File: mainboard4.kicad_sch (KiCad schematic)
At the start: 14 parts, among them J13 USB_C_Receptacle_USB2.0_16P, J8 Barrel_Jack

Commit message: change cad data
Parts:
- removed C103, C104: 0.1uF, Capacitor_SMD:C_0402_1005Metric_Pad0.74x0.62mm_HandSolder, symbol Device:C
- renumbered C80 to C107, C81 to C108, C82 to C109, C83 to C110, C101 to C125, C102 to C126, C42 to C64, C43 to C65, C44 to C66, C45 to C67
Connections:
- net USB HUB/SS_RX_N is gone; now on net USB HUB/SS_TX_N: C126.1
- net USB HUB/SS_RX_P is gone; now on net USB HUB/SS_TX_P: C125.1
- net Ethernet PHY/RXN: now also C66.2; no longer C64.2
- net Ethernet PHY/RXP: now also C67.2; no longer C65.2
- net Ethernet PHY/TXN: now also C64.2; no longer C66.2
- net Ethernet PHY/TXP: now also C65.2; no longer C67.2
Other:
- added sheet IMU (imu.kicad_sch)
- sheet MCU ports: added CS, INT, MISO, MOSI, RST, SCLK, USB_DN, USB_DP; removed none
- sheet USB2Ethernet ports: added USB2DM, USB2DP; removed none
- moved on the sheet: C107, C109, C110, C125, C126, C64, C65, C66, C67, J13, J8

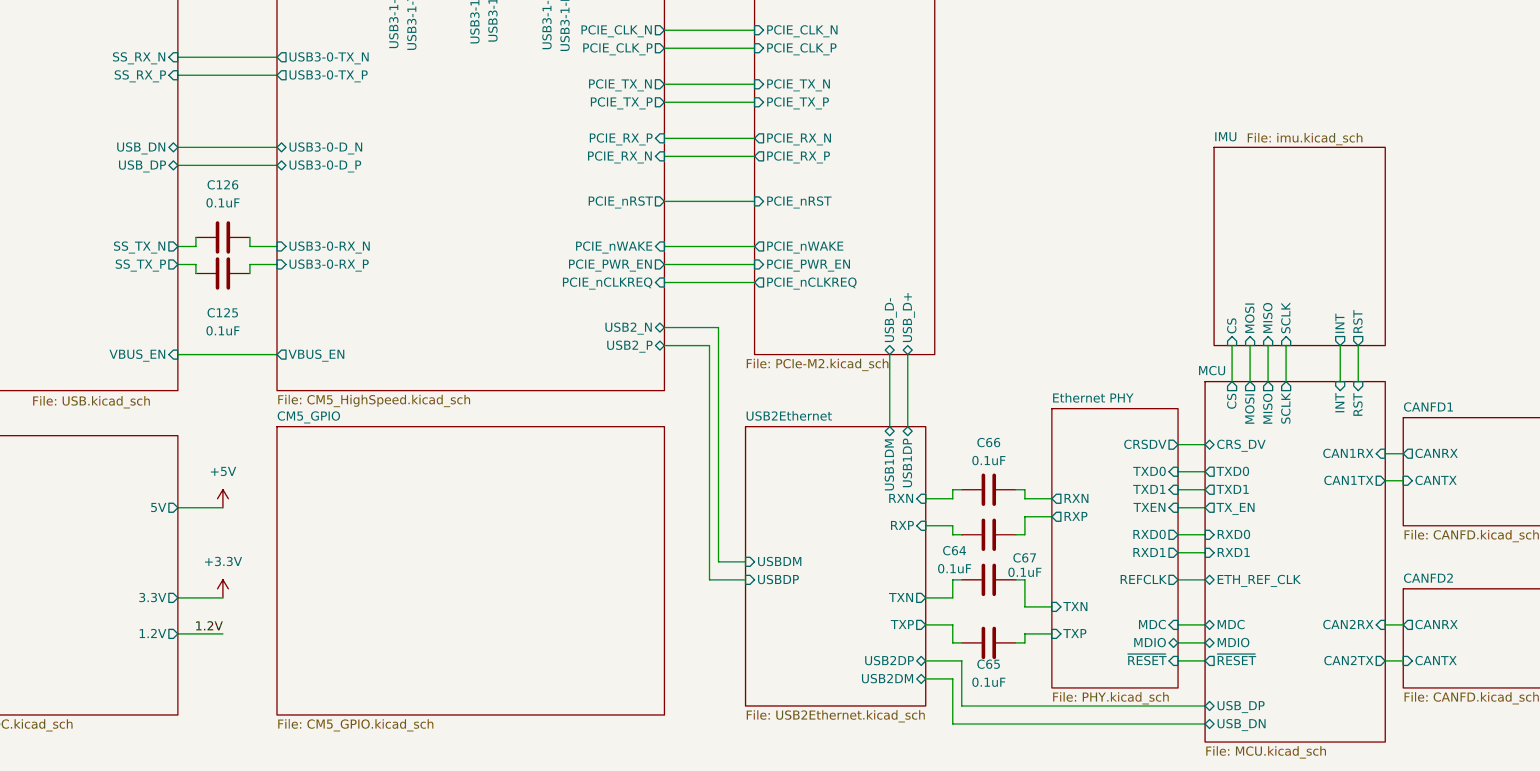
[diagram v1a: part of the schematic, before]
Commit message: change clearance
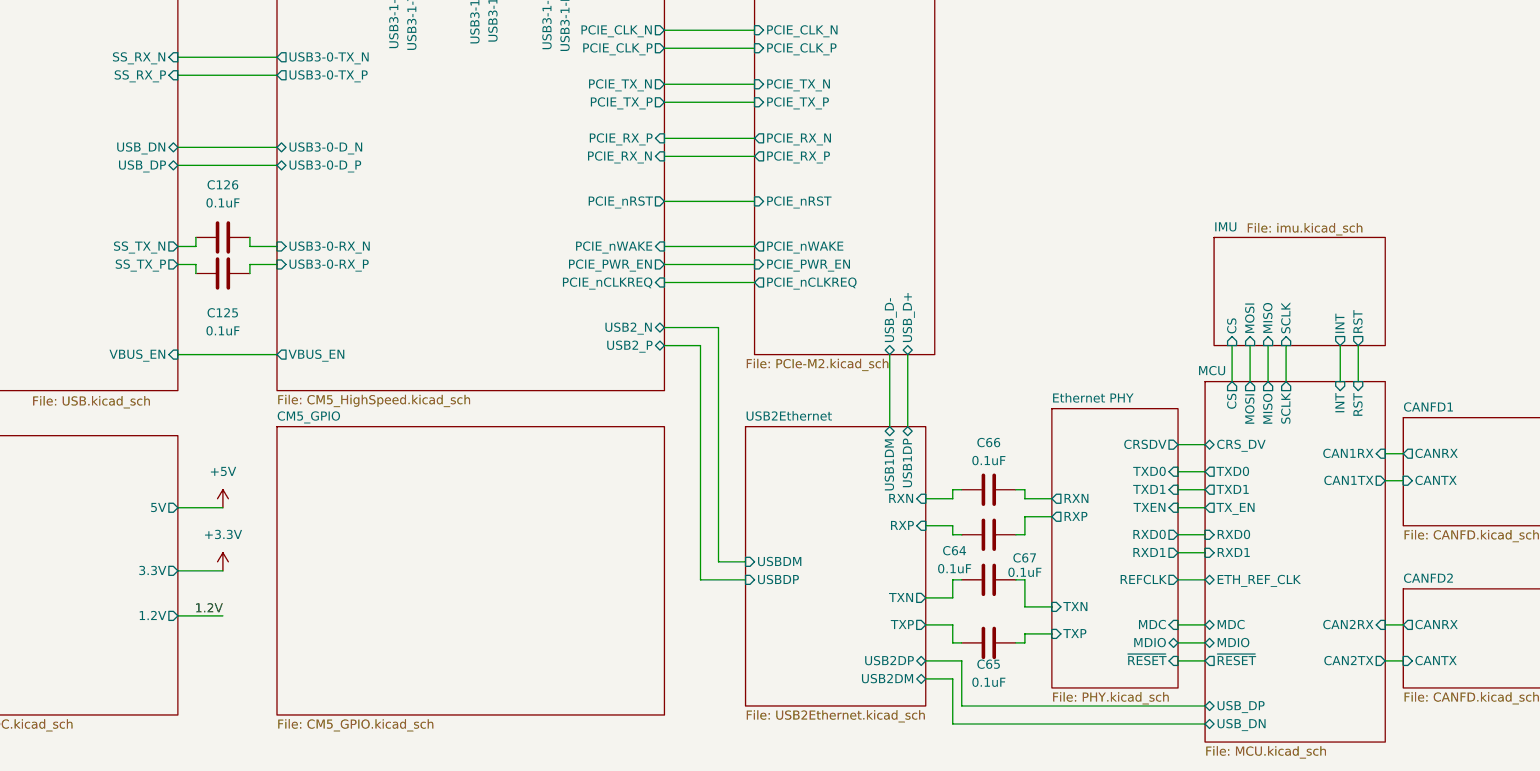
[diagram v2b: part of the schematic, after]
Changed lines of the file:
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@@
 	(wire
 		(pts
-			(xy 156.21 110.49) (xy 149.86 110.49)
+			(xy 154.94 110.49) (xy 149.86 110.49)
 		)
 		(stroke
@@
 	(wire
 		(pts
-			(xy 81.28 146.05) (xy 87.63 146.05)
+			(xy 81.28 142.24) (xy 87.63 142.24)
 		)
 		(stroke
@@
 	(wire
 		(pts
-			(xy 161.29 143.51) (xy 156.21 143.51)
+			(xy 161.29 143.51) (xy 154.94 143.51)
 		)
 		(stroke
@@
 	(wire
 		(pts
-			(xy 81.28 151.13) (xy 87.63 151.13)
+			(xy 81.28 148.59) (xy 87.63 148.59)
 		)
 		(stroke
@@
 	(wire
 		(pts
-			(xy 156.21 110.49) (xy 156.21 143.51)
+			(xy 154.94 110.49) (xy 154.94 143.51)
 		)
 		(stroke
@@
 	)
 	(label "1.2V"
-		(at 87.63 151.13 180)
+		(at 87.63 148.59 180)
 		(fields_autoplaced yes)
 		(effects
@@
 	(symbol
 		(lib_id "power:+3.3V")
-		(at 87.63 146.05 0)
+		(at 87.63 142.24 0)
 		(unit 1)
 		(exclude_from_sim no)
@@
 		(fields_autoplaced yes)
 		(property "Reference" "#PWR0105"
-			(at 87.63 149.86 0)
+			(at 87.63 146.05 0)
 			(effects
 				(font
@@
 		)
 		(property "Value" "+3.3V"
-			(at 87.63 140.97 0)
+			(at 87.63 137.16 0)
 			(effects
 				(font
@@
 		)
 		(property "Footprint" ""
-			(at 87.63 146.05 0)
+			(at 87.63 142.24 0)
 			(effects
 				(font
@@
 		)
 		(property "Datasheet" ""
-			(at 87.63 146.05 0)
+			(at 87.63 142.24 0)
 			(effects
 				(font
@@
 		)
 		(property "Description" "Power symbol creates a global label with name \"+3.3V\""
-			(at 87.63 146.05 0)
+			(at 87.63 142.24 0)
 			(effects
 				(font
@@
 	)
 	(sheet
-		(at 227.33 82.55)
-		(size 24.13 27.94)
+		(at 227.33 95.25)
+		(size 24.13 15.24)
 		(stroke
 			(width 0.1524)
@@
 		)
 		(property "Sheetname" "IMU"
-			(at 227.33 81.8384 0)
+			(at 227.33 94.5384 0)
 			(effects
 				(font
@@
 		)
 		(property "Sheetfile" "imu.kicad_sch"
-			(at 231.902 80.518 0)
+			(at 231.902 93.218 0)
 			(effects
 				(font
@@
 		)
 		(pin "3.3V" output
-			(at 81.28 146.05 0)
+			(at 81.28 142.24 0)
 			(effects
 				(font
@@
 		)
 		(pin "1.2V" output
-			(at 81.28 151.13 0)
+			(at 81.28 148.59 0)
 			(effects
 				(font

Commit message: remove efuse
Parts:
- renumbered C110 to C100, C125 to C115, C126 to C116, C64 to C54, C65 to C55, C66 to C56, C67 to C57, C107 to C97, C108 to C98, C109 to C99
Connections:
- net Power/VBUS renamed +12V
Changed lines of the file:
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@@
 		(on_board yes)
 		(dnp no)
-		(property "Reference" "C125"
+		(property "Reference" "C115"
 			(at 87.63 105.918 90)
 			(effects
@@
 			(project "mainboard4"
 				(path "/dd07ab80-a59c-44f4-ac7d-849e21e1384e"
-					(reference "C125")
+					(reference "C115")
 					(unit 1)
 				)
@@
 		(on_board yes)
 		(dnp no)
-		(property "Reference" "C109"
+		(property "Reference" "C99"
 			(at 119.126 42.164 0)
 			(effects
@@
 			(project "mainboard4"
 				(path "/dd07ab80-a59c-44f4-ac7d-849e21e1384e"
-					(reference "C109")
+					(reference "C99")
 					(unit 1)
 				)
@@
 		(on_board yes)
 		(dnp no)
-		(property "Reference" "C126"
+		(property "Reference" "C116"
 			(at 87.63 87.884 90)
 			(effects
@@
 			(project "mainboard4"
 				(path "/dd07ab80-a59c-44f4-ac7d-849e21e1384e"
-					(reference "C126")
+					(reference "C116")
 					(unit 1)
 				)
@@
 		(on_board yes)
 		(dnp no)
-		(property "Reference" "C65"
+		(property "Reference" "C55"
 			(at 195.58 155.448 90)
 			(effects
@@
 			(project "mainboard4"
 				(path "/dd07ab80-a59c-44f4-ac7d-849e21e1384e"
-					(reference "C65")
+					(reference "C55")
 					(unit 1)
 				)
@@
 		(on_board yes)
 		(dnp no)
-		(property "Reference" "C66"
+		(property "Reference" "C56"
 			(at 195.58 124.206 90)
 			(effects
@@
 			(project "mainboard4"
 				(path "/dd07ab80-a59c-44f4-ac7d-849e21e1384e"
-					(reference "C66")
+					(reference "C56")
 					(unit 1)
 				)
@@
 		(on_board yes)
 		(dnp no)
-		(property "Reference" "C107"
+		(property "Reference" "C97"
 			(at 143.51 47.752 0)
 			(effects
@@
 			(project "mainboard4"
 				(path "/dd07ab80-a59c-44f4-ac7d-849e21e1384e"
-					(reference "C107")
+					(reference "C97")
 					(unit 1)
 				)
@@
 		(on_board yes)
 		(dnp no)
-		(property "Reference" "C110"
+		(property "Reference" "C100"
 			(at 104.14 48.26 0)
 			(effects
@@
 			(project "mainboard4"
 				(path "/dd07ab80-a59c-44f4-ac7d-849e21e1384e"
-					(reference "C110")
+					(reference "C100")
+					(unit 1)
+				)
+			)
+		)
+	)
+	(symbol
+		(lib_id "power:+12V")
+		(at 43.18 128.27 0)
+		(unit 1)
+		(exclude_from_sim no)
+		(in_bom yes)
+		(on_board yes)
+		(dnp no)
+		(fields_autoplaced yes)
+		(property "Reference" "#PWR038"
+			(at 43.18 132.08 0)
+			(effects
+				(font
+					(size 1.27 1.27)
+				)
+				(hide yes)
+			)
+		)
+		(property "Value" "+12V"
+			(at 43.18 123.19 0)
+			(effects
+				(font
+					(size 1.27 1.27)
+				)
+			)
+		)
+		(property "Footprint" ""
+			(at 43.18 128.27 0)
+			(effects
+				(font
+					(size 1.27 1.27)
+				)
+				(hide yes)
+			)
+		)
+		(property "Datasheet" ""
+			(at 43.18 128.27 0)
+			(effects
+				(font
+					(size 1.27 1.27)
+				)
+				(hide yes)
+			)
+		)
+		(property "Description" "Power symbol creates a global label with name \"+12V\""
+			(at 43.18 128.27 0)
+			(effects
+				(font
+					(size 1.27 1.27)
+				)
+				(hide yes)
+			)
+		)
+		(pin "1"
+		)
+		(instances
+			(project "mainboard4"
+				(path "/dd07ab80-a59c-44f4-ac7d-849e21e1384e"
+					(reference "#PWR038")
 					(unit 1)
 				)
@@
 		(on_board yes)
 		(dnp no)
-		(property "Reference" "C64"
+		(property "Reference" "C54"
 			(at 190.754 139.446 90)
 			(effects
@@
 			(project "mainboard4"
 				(path "/dd07ab80-a59c-44f4-ac7d-849e21e1384e"
-					(reference "C64")
+					(reference "C54")
 					(unit 1)
 				)
@@
 		(on_board yes)
 		(dnp no)
-		(property "Reference" "C108"
+		(property "Reference" "C98"
 			(at 130.81 52.07 0)
 			(effects
@@
 			(project "mainboard4"
 				(path "/dd07ab80-a59c-44f4-ac7d-849e21e1384e"
-					(reference "C108")
+					(reference "C98")
 					(unit 1)
 				)
@@
 		(on_board yes)
 		(dnp no)
-		(property "Reference" "C67"
+		(property "Reference" "C57"
 			(at 200.66 140.462 90)
 			(effects
@@
 			(project "mainboard4"
 				(path "/dd07ab80-a59c-44f4-ac7d-849e21e1384e"
-					(reference "C67")
-					(unit 1)
-				)
+					(reference "C57")
+					(unit 1)
+				)

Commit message: change design
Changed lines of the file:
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@@
 	(label "1.2V"
 		(at 41.91 104.14 0)
-		(fields_autoplaced yes)
 		(effects
 			(font
@@
 	(label "1.2V"
 		(at 87.63 148.59 180)
-		(fields_autoplaced yes)
 		(effects
 			(font
@@
 	(sheet
 		(at 226.06 115.57)
-		(size 25.4 50.8)
+		(size 25.4 49.53)
 		(stroke
 			(width 0.1524)
@@
 		)
 		(property "Sheetfile" "MCU.kicad_sch"
-			(at 226.06 166.9546 0)
-			(effects
-				(font
+			(at 230.886 165.608 0)
+			(effects
+				(font
